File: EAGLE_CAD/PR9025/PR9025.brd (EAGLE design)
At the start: 70 x 70 mm, 67 parts, among them SW1 C&K_PTS645

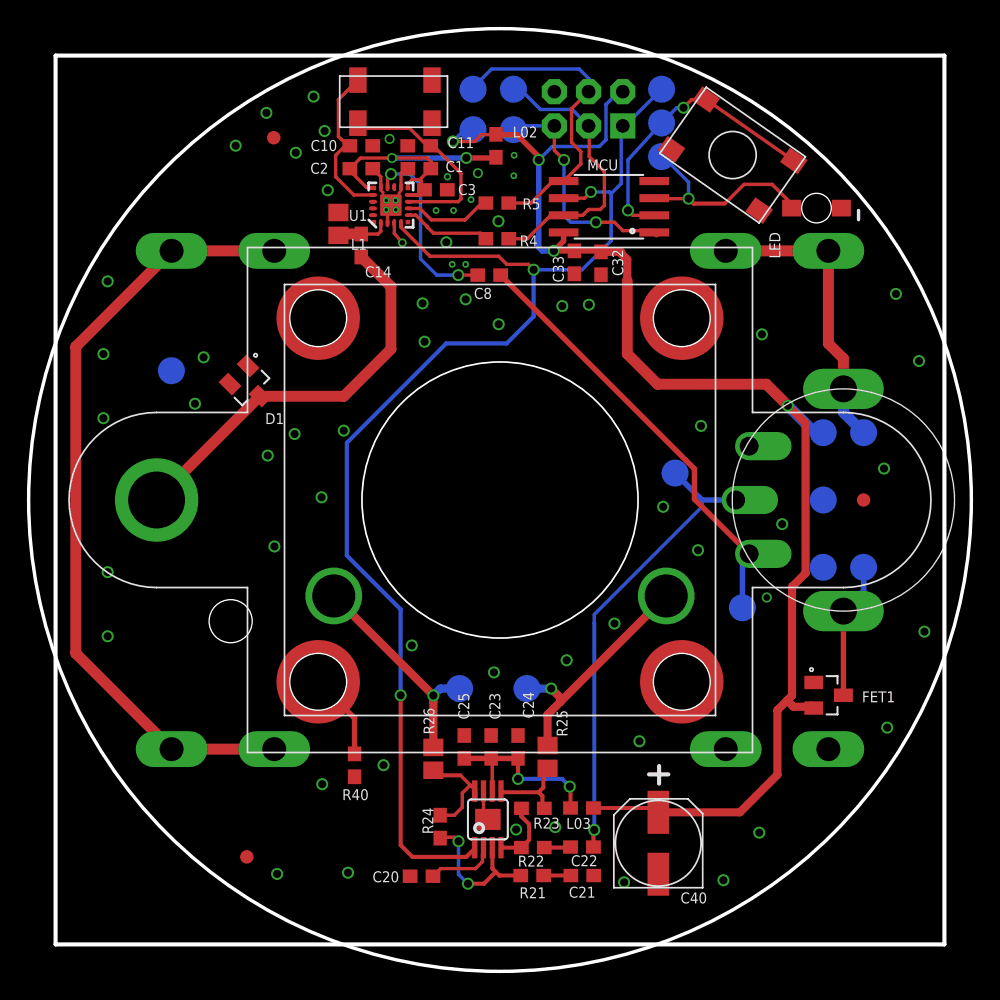
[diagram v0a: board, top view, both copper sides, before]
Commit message: PR9025
Updated DFM rework from Josh
- removed R4 & R5
- FM_IC Sen tied high

Simplified board dimension outline
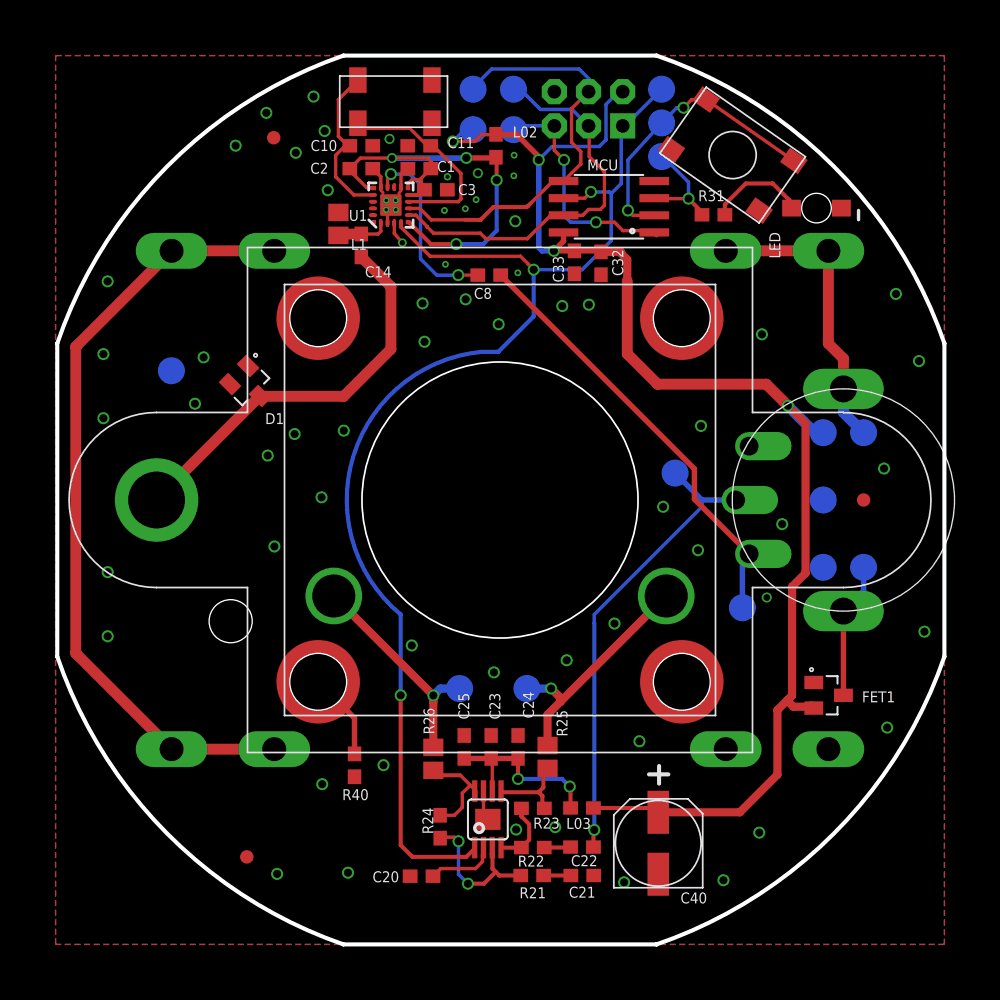
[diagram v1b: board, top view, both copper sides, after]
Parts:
- removed R4, R5: 330, PR_Parts_Library:0603_CPL
- added R31: 1K, PR_Parts_Library:0603_CPL
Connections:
- removed net SCLK-L: R4.2, U1.7
- removed net SDIO-L: R5.2, U1.8
- new net N$7: LED.P$1, R31.2
- net 3.3V: now also U1.6
- net LED/PB4: now also R31.1; no longer LED.P$1
- net SCLK: now also U1.7; no longer R4.1
- net SDIO: now also U1.8; no longer R5.1
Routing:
- net 3.3V: track 23.7 -> 36.8 mm, vias 2 -> 4
- net SDIO: track 23.3 -> 31.6 mm
- net SCLK: track 21.2 -> 29.4 mm
- net LED/PB4: track 16.3 -> 8.18 mm
- net N$7: track 0.00 -> 7.36 mm
- net !RST: track 94.0 -> 87.3 mm
- net SDIO-L: track 6.65 -> 0.00 mm
- net SCLK-L: track 6.45 -> 0.00 mm
- net GND: vias 66 -> 65
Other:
- board size 70 x 70 mm -> 65.9 x 66 mm
